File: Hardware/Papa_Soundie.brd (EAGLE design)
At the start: 38.1 x 63.5 mm, 79 parts, among them J1 Audio Jack, J2 MICRO-SD_CARD_SOCKET, U1 ATMEGA328P_TQFP, U2 VS1000D, U3 3.3V, U4 4MB Flash, Y1 12MHz, Y2 8MHz

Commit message: final layout
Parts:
- J6: device SparkFun-Connectors:1X07 -> SparkFun-Connectors:1X05
- J8: device SparkFun-Connectors:1X04 -> SparkFun-Connectors:1X02
- moved LOGO6 87.6 mm to (30.9, 42.6), turned to 0 degrees
- moved LOGO1 87.1 mm to (19.0, 31.2), turned to 0 degrees
- moved LOGO2 66.6 mm to (33.5, 4.06)
- moved J7 48.5 mm to (1.27, 44.5)
- moved J8 39.8 mm to (1.27, 57.1), turned to 270 degrees
- moved J5 38.7 mm to (36.8, 31.8), turned to 90 degrees
- moved J10 37.8 mm to (36.8, 26.7)
- moved J11 37.8 mm to (36.8, 21.6)
- moved J3 37.8 mm to (36.8, 16.5)
- moved C16 27.1 mm to (8.10, 61.6), turned to 0 degrees
- moved R16 26.2 mm to (30.8, 24.0), turned to 180 degrees
- moved R32 24.2 mm to (23.3, 42.1), turned to 90 degrees
- moved LOGO3 24.1 mm to (35.7, 12.2)
- moved Y1 23.4 mm to (31.9, 37.8), turned to 180 degrees
- moved S1 22.8 mm to (8.73, 43.0), turned to 0 degrees
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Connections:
- removed net A2: J8.3, U1.25
- removed net A3: J8.4, U1.26
- removed net D7: J6.7, U1.11
- removed net D8: J6.6, U1.12
- net USBN: now also J10.2; no longer J10.1
- net USBP: now also J10.1; no longer J10.2
- net VS_RX: now also J11.2; no longer J11.1
- net VS_TX: now also J11.1; no longer J11.2
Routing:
- net VCC: track 69.4 -> 173.9 mm, vias 4 -> 13
- net DVDD: track 43.1 -> 131.8 mm, vias 0 -> 6
- net SCL: track 66.5 -> 12.6 mm, vias 1 -> 0
- net SDA: track 60.1 -> 10.9 mm, vias 1 -> 0
- net RAW: track 27.2 -> 70.1 mm, vias 1 -> 2
- net L_AC: track 57.1 -> 17.2 mm, vias 1 -> 0
- net D7: track 36.5 -> 0.00 mm
- net LEFT: track 6.05 -> 41.1 mm
- net D8: track 33.9 -> 0.00 mm
- net RIGHT: track 5.89 -> 37.2 mm, vias 0 -> 2
- net N$31: track 25.9 -> 54.6 mm, vias 2 -> 4
- net USBN: track 0.87 -> 26.9 mm, vias 0 -> 2
- net A2: track 24.6 -> 0.00 mm
- net GBUF: track 27.8 -> 3.68 mm, vias 2 -> 0
- net A3: track 24.0 -> 0.00 mm
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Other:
- board text added: "3.3V"
- board text added: "LEFT_AC"
- board text added: "MISO D12"
- board text added: "MOSI D11"
- board text added: "RIGHT_AC"
- board text added: "RST"
- board text added: "RX"
- board text added: "SCK D13"
- board text added: "TX"
- board text added: "UN"
- board text added: "UP"
- board text added: "USBN"
- board text added: "USBP"
- board text added: "VS_RX"
- board text added: "VS_TX"
- board text removed: "3.3"
- board text removed: "3.6-5.5v"
- board text removed: "A2"
- board text removed: "A3"
- board text removed: "AUDIO PLAYER"
- board text removed: "D11"
- board text removed: "D12"
- board text removed: "D13"
- board text removed: "D7"
- board text removed: "D8"
- board text removed: "LIL' SOUNDIE"
- board text removed: "MISO"
- board text removed: "MOSI"
- board text removed: "RESET"
- board text removed: "SCK"
- board text removed: "VCC"
- board text removed: "~"

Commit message: added pull-up resistor on XCS line
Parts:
- added R25: 100k, SparkFun-Resistors:0603-RES
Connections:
- net DVDD: now also R25.2
- net XCS: now also R25.1
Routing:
- net DVDD: track 131.8 -> 134.2 mm
- net XCS: track 24.3 -> 23.5 mm
- net GND: vias 53 -> 54
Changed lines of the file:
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@@
 <element name="J5" library="SparkFun-Connectors" package="1X02" value="" x="36.83" y="31.75" rot="R90"/>
 <element name="J10" library="SparkFun-Connectors" package="1X02" value="" x="36.83" y="26.67" rot="R90"/>
+<element name="R25" library="SparkFun-Resistors" package="0603-RES" value="100k" x="23.33625" y="22.86">
+<attribute name="PROD_ID" value="RES-07828" x="23.33625" y="22.86" size="1.778" layer="27" display="off"/>
+</element>
 </elements>
 <signals>
@@
 <via x="20.47875" y="26.67" extent="1-16" drill="0.381"/>
 <via x="23.8125" y="25.24125" extent="1-16" drill="0.381"/>
-<via x="23.1775" y="22.38375" extent="1-16" drill="0.381"/>
+<via x="22.38375" y="21.11375" extent="1-16" drill="0.381"/>
 <via x="34.925" y="22.70125" extent="1-16" drill="0.381"/>
 <via x="32.22625" y="57.30875" extent="1-16" drill="0.381"/>
@@
 <via x="1.27" y="42.38625" extent="1-16" drill="0.381"/>
 <via x="0.79375" y="20.79625" extent="1-16" drill="0.381"/>
+<via x="19.05" y="20.32" extent="1-16" drill="0.381"/>
 </signal>
 <signal name="PWRBTN">
@@
 <wire x1="19.685" y1="16.8275" x2="20.0025" y2="17.145" width="0.2032" layer="1"/>
 <wire x1="20.0025" y1="17.145" x2="20.955" y2="17.145" width="0.2032" layer="1"/>
-<wire x1="20.955" y1="17.145" x2="25.55875" y2="21.74875" width="0.2032" layer="1"/>
+<wire x1="20.955" y1="17.145" x2="24.4475" y2="20.6375" width="0.2032" layer="1"/>
+<wire x1="24.4475" y1="20.6375" x2="25.55875" y2="21.74875" width="0.2032" layer="1"/>
 <wire x1="18.57375" y1="17.93875" x2="19.685" y2="16.8275" width="0.2032" layer="1"/>
 <wire x1="17.93875" y1="19.31125" x2="17.93875" y2="17.93875" width="0.2032" layer="1"/>
@@
 <wire x1="21.0775" y1="33.56375" x2="22.56" y2="33.56375" width="0.2032" layer="1"/>
 <wire x1="22.56" y1="33.56375" x2="22.77125" y2="33.775" width="0.2032" layer="1"/>
+<contactref element="R25" pad="2"/>
+<wire x1="24.18625" y1="22.86" x2="24.18625" y2="20.89875" width="0.2032" layer="1"/>
+<wire x1="24.18625" y1="20.89875" x2="24.4475" y2="20.6375" width="0.2032" layer="1"/>
 </signal>
 <signal name="N$2">
@@
 <wire x1="18.0775" y1="29.56375" x2="18.0775" y2="28.595" width="0.2032" layer="1"/>
 <wire x1="18.0775" y1="28.595" x2="18.57375" y2="28.09875" width="0.2032" layer="1"/>
-<via x="19.52625" y="23.495" extent="1-16" drill="0.381"/>
+<via x="19.3675" y="23.33625" extent="1-16" drill="0.381"/>
 <via x="10.16" y="22.38375" extent="1-16" drill="0.381"/>
 <wire x1="10.16" y1="22.38375" x2="10.16" y2="21.17" width="0.2032" layer="1"/>
@@
 <wire x1="10.16" y1="22.38375" x2="10.16" y2="27.305" width="0.2032" layer="16"/>
 <wire x1="10.16" y1="27.305" x2="10.4775" y2="27.6225" width="0.2032" layer="16"/>
-<wire x1="18.57375" y1="28.09875" x2="18.57375" y2="24.4475" width="0.2032" layer="1"/>
-<wire x1="18.57375" y1="24.4475" x2="19.52625" y2="23.495" width="0.2032" layer="1"/>
-<wire x1="18.0975" y1="24.92375" x2="19.52625" y2="23.495" width="0.2032" layer="16"/>
-<wire x1="18.0975" y1="24.92375" x2="18.0975" y2="27.14625" width="0.2032" layer="16"/>
+<wire x1="18.57375" y1="28.09875" x2="18.57375" y2="24.13" width="0.2032" layer="1"/>
+<wire x1="18.0975" y1="24.60625" x2="18.0975" y2="27.14625" width="0.2032" layer="16"/>
 <wire x1="18.0975" y1="27.14625" x2="17.62125" y2="27.6225" width="0.2032" layer="16"/>
 <wire x1="17.62125" y1="27.6225" x2="10.4775" y2="27.6225" width="0.2032" layer="16"/>
+<wire x1="18.57375" y1="24.13" x2="19.3675" y2="23.33625" width="0.2032" layer="1"/>
+<wire x1="18.0975" y1="24.60625" x2="19.3675" y2="23.33625" width="0.2032" layer="16"/>
 </signal>
 <signal name="IO_0">
@@
 <wire x1="18.5775" y1="29.56375" x2="18.5775" y2="28.73" width="0.2032" layer="1"/>
 <wire x1="18.5775" y1="28.73" x2="19.20875" y2="28.09875" width="0.2032" layer="1"/>
-<wire x1="19.20875" y1="28.09875" x2="19.20875" y2="24.92375" width="0.2032" layer="1"/>
-<via x="21.74875" y="23.01875" extent="1-16" drill="0.381"/>
+<via x="20.79625" y="24.4475" extent="1-16" drill="0.381"/>
 <via x="25.0825" y="30.12375" extent="1-16" drill="0.381"/>
 <wire x1="27.26725" y1="30.00375" x2="27.33075" y2="30.06725" width="0.2032" layer="1"/>
 <wire x1="23.8125" y1="30.00375" x2="21.9075" y2="28.09875" width="0.2032" layer="16"/>
-<wire x1="20.955" y1="23.8125" x2="21.74875" y2="23.01875" width="0.2032" layer="16"/>
-<wire x1="19.20875" y1="24.92375" x2="19.52625" y2="24.60625" width="0.2032" layer="1"/>
-<wire x1="19.52625" y1="24.60625" x2="20.16125" y2="24.60625" width="0.2032" layer="1"/>
-<wire x1="20.16125" y1="24.60625" x2="21.74875" y2="23.01875" width="0.2032" layer="1"/>
 <wire x1="21.9075" y1="28.09875" x2="19.52625" y2="28.09875" width="0.2032" layer="16"/>
 <wire x1="19.52625" y1="28.09875" x2="19.20875" y2="27.78125" width="0.2032" layer="16"/>
-<wire x1="19.20875" y1="27.78125" x2="19.20875" y2="25.55875" width="0.2032" layer="16"/>
-<wire x1="19.20875" y1="25.55875" x2="21.74875" y2="23.01875" width="0.2032" layer="16"/>
 <wire x1="23.8125" y1="30.00375" x2="24.9625" y2="30.00375" width="0.2032" layer="16"/>
 <wire x1="24.9625" y1="30.00375" x2="25.0825" y2="30.12375" width="0.2032" layer="16"/>
 <wire x1="27.26725" y1="30.00375" x2="25.2025" y2="30.00375" width="0.2032" layer="1"/>
 <wire x1="25.2025" y1="30.00375" x2="25.0825" y2="30.12375" width="0.2032" layer="1"/>
+<contactref element="R25" pad="1"/>
+<wire x1="21.2725" y1="22.86" x2="22.48625" y2="22.86" width="0.2032" layer="1"/>
+<wire x1="19.20875" y1="24.92375" x2="19.685" y2="24.4475" width="0.2032" layer="16"/>
+<wire x1="21.2725" y1="22.86" x2="20.955" y2="23.1775" width="0.2032" layer="1"/>
+<wire x1="20.955" y1="23.1775" x2="20.955" y2="24.28875" width="0.2032" layer="1"/>
+<wire x1="20.955" y1="24.28875" x2="20.79625" y2="24.4475" width="0.2032" layer="1"/>
+<wire x1="19.20875" y1="27.78125" x2="19.20875" y2="24.92375" width="0.2032" layer="16"/>
+<wire x1="19.685" y1="24.4475" x2="20.79625" y2="24.4475" width="0.2032" layer="16"/>
+<wire x1="19.20875" y1="28.09875" x2="19.20875" y2="24.92375" width="0.2032" layer="1"/>
+<wire x1="19.20875" y1="24.92375" x2="19.605625" y2="24.526875" width="0.2032" layer="1"/>
+<wire x1="19.605625" y1="24.526875" x2="20.716875" y2="24.526875" width="0.2032" layer="1"/>
+<wire x1="20.716875" y1="24.526875" x2="20.79625" y2="24.4475" width="0.2032" layer="1"/>
 </signal>
 <signal name="SCLK">

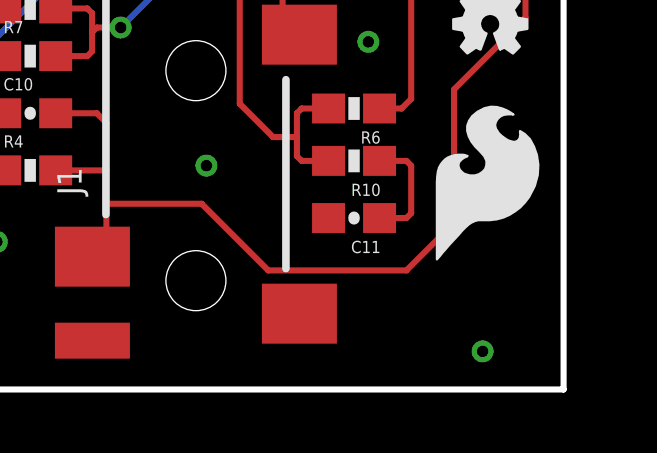
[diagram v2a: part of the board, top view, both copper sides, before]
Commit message: added measurement to third standoff
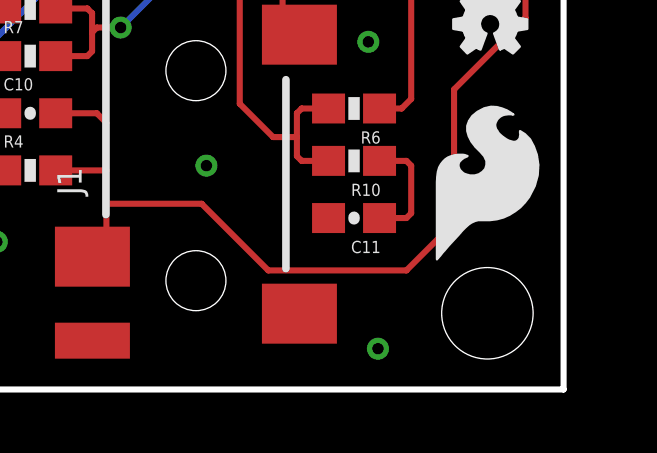
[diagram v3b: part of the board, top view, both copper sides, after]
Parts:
- added H3: STAND-OFFTIGHT, SparkFun-Electromechanical:STAND-OFF-TIGHT
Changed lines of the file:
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@@
 <setting verticaltext="up"/>
 </settings>
-<grid distance="0.00625" unitdist="inch" unit="inch" style="lines" multiple="1" display="yes" altdistance="0.01" altunitdist="mm" altunit="mm"/>
+<grid distance="0.05" unitdist="inch" unit="inch" style="lines" multiple="1" display="yes" altdistance="0.01" altunitdist="mm" altunit="mm"/>
 <layers>
 <layer number="1" name="Top" color="4" fill="1" visible="yes" active="yes"/>
@@
 <layer number="45" name="Holes" color="7" fill="1" visible="no" active="yes"/>
 <layer number="46" name="Milling" color="3" fill="1" visible="no" active="yes"/>
-<layer number="47" name="Measures" color="7" fill="1" visible="no" active="yes"/>
+<layer number="47" name="Measures" color="7" fill="1" visible="yes" active="yes"/>
 <layer number="48" name="Document" color="7" fill="1" visible="no" active="yes"/>
 <layer number="49" name="Reference" color="7" fill="1" visible="yes" active="yes"/>
@@
 <text x="28.32625" y="17.005" size="1.016" layer="22" font="vector" ratio="20" rot="MR180">RIGHT_AC</text>
 <wire x1="2.54" y1="58.26125" x2="2.69875" y2="58.26125" width="0.2032" layer="49"/>
+<dimension x1="35.56" y1="2.54" x2="38.1" y2="2.54" x3="36.83" y3="-3.81" textsize="1.778" layer="47" unit="inch"/>
 </plain>
 <attributes>
@@
 <attribute name="PROD_ID" value="RES-07828" x="23.33625" y="22.86" size="1.778" layer="27" display="off"/>
 </element>
+<element name="H3" library="SparkFun-Electromechanical" package="STAND-OFF-TIGHT" value="STAND-OFFTIGHT" x="35.56" y="2.54"/>
 </elements>
 <signals>
@@
 <via x="26.19375" y="7.46125" extent="1-16" drill="0.381"/>
 <via x="34.44875" y="15.875" extent="1-16" drill="0.381"/>
-<via x="35.40125" y="1.27" extent="1-16" drill="0.381"/>
+<via x="31.91125" y="1.36" extent="1-16" drill="0.381"/>
 <via x="14.605" y="46.6725" extent="1-16" drill="0.381"/>
 <via x="15.71625" y="49.05375" extent="1-16" drill="0.381"/>

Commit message: changes per QC Review
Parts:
- moved C4 17.3 mm to (16.3, 42.4), turned to 90 degrees
- moved C7 1.15 mm to (14.3, 42.4)
- moved R27 0.51 mm to (18.0, 42.2)
- moved C15 0.38 mm to (19.7, 42.2)
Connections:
- net AVDD: now also C4.1
- net VCC: no longer C4.1
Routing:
- net N$2: track 4.15 -> 0.00 mm
- net VCC: track 173.9 -> 171.9 mm
- net AVDD: track 13.6 -> 15.0 mm
- net N$7: track 3.39 -> 3.99 mm
- net GBUF: track 3.68 -> 4.19 mm
- net GND: vias 54 -> 55

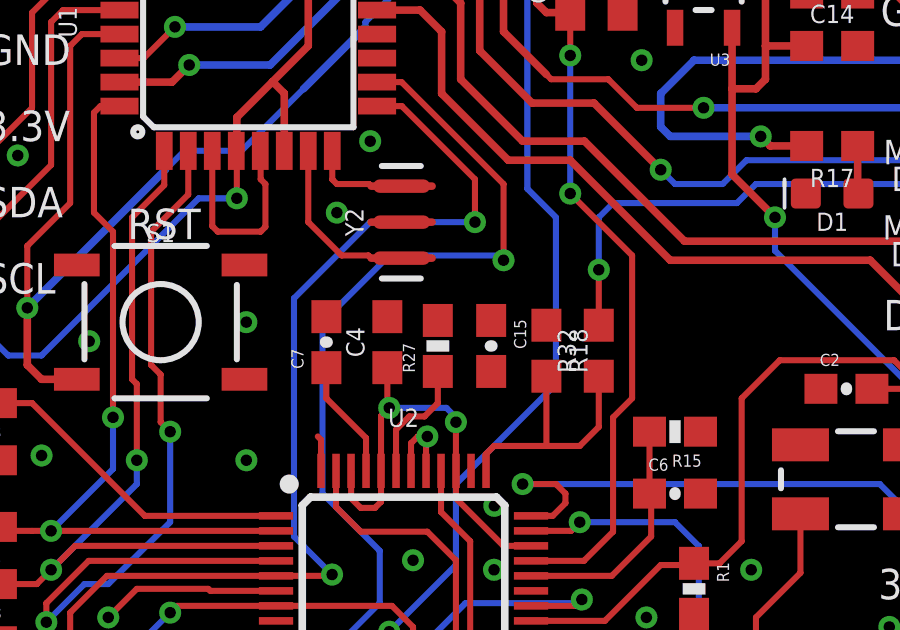
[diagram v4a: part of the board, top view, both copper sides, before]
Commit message: Fixing issues per QC review
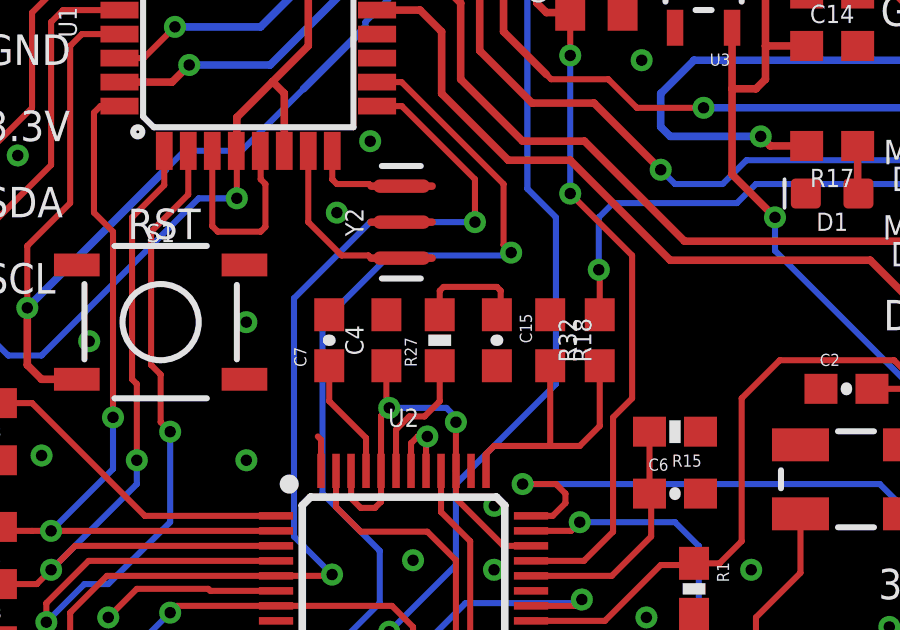
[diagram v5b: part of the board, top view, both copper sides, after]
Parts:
- moved R18 0.37 mm to (21.7, 42.4)
- moved R32 0.35 mm to (23.4, 42.4)
- moved C15 0.27 mm to (19.9, 42.4)
- moved R27 0.20 mm to (18.0, 42.4)
- moved C7 0.11 mm to (14.4, 42.4)
- moved C4 0.07 mm to (16.3, 42.4)
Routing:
- net N$2: track 0.00 -> 3.79 mm
- net PWRBTN: track 8.71 -> 9.42 mm

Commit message: Updated design for rev 2
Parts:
- removed C27: 1.0uF, SparkFun-Capacitors:0603
- removed R32: 39k, SparkFun-Resistors:0603
- added D2, D3: RED, SparkFun-LED:LED-0603
- added J12: (no value), SparkFun-Connectors:1X01
- added R26: 2.0k, SparkFun-Resistors:0603
- R18: value 68.1k -> 2.0k
- moved R18 18.2 mm to (8.64, 29.7), turned to 0 degrees
- moved FD3 5.97 mm to (5.71, 61.8)
- moved FD1 1.41 mm to (5.71, 61.8)
- moved R11 0.90 mm to (2.41, 25.8)
- moved R12 0.90 mm to (2.41, 35.3)
- moved R22 0.90 mm to (2.41, 23.9)
- moved R29 0.90 mm to (2.41, 31.5)
- moved R30 0.90 mm to (2.41, 29.6)
- moved R31 0.90 mm to (2.41, 27.7)
- moved C13 0.90 mm to (2.41, 39.4)
- moved R23 0.90 mm to (2.41, 37.5)
- moved R28 0.90 mm to (2.41, 33.4)
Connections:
- removed net N$60: C27.2, R32.2
- new net N$34: D2.C, R18.2
- new net N$35: D2.A, U2.10
- new net N$36: D3.C, R26.2
- new net RST: C8.2, J12.1, R9.1, S1.3, U1.29
- net GND: now also C3.2, J2.CD2, R26.1
- net N$31: now also D3.A, U1.25; no longer C8.2, R9.1, S1.3, U1.29
- net PWRBTN: now also U1.11; no longer R18.2, R32.1
- net RAW: no longer C27.1
- net SD3V3: no longer C3.2
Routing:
- net RST: track 0.00 -> 58.2 mm, vias 0 -> 4
- net N$31: track 54.6 -> 6.72 mm, vias 4 -> 0
- net N$60: track 23.7 -> 0.00 mm, vias 2 -> 0
- net PWRBTN: track 9.42 -> 18.8 mm, vias 0 -> 2
- net N$35: track 0.00 -> 3.28 mm
- net RAW: track 70.1 -> 67.7 mm
- net N$34: track 0.00 -> 2.23 mm
- net GND: track 26.2 -> 28.0 mm, vias 55 -> 56
- net IO_4: track 42.0 -> 43.5 mm
- net N$36: track 0.00 -> 1.45 mm
- net A0: track 10.7 -> 11.7 mm, vias 0 -> 1
- net SD3V3: track 38.9 -> 37.8 mm
- net IO_3: track 36.4 -> 37.4 mm
- net IO_6: track 12.2 -> 12.8 mm
- net IO_7: track 12.8 -> 13.4 mm
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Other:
- board text added: "RDY"
- board text added: "VLSI RDY"
- board text added: "v03"
- board text removed: "v02"

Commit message: Updated Version No., removed ground connection from SD Card, v03
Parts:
- moved LOGO3 35.9 mm to (8.60, 35.8)
- moved LOGO2 32.3 mm to (7.24, 22.9)
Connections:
- net GND: no longer J2.CD2

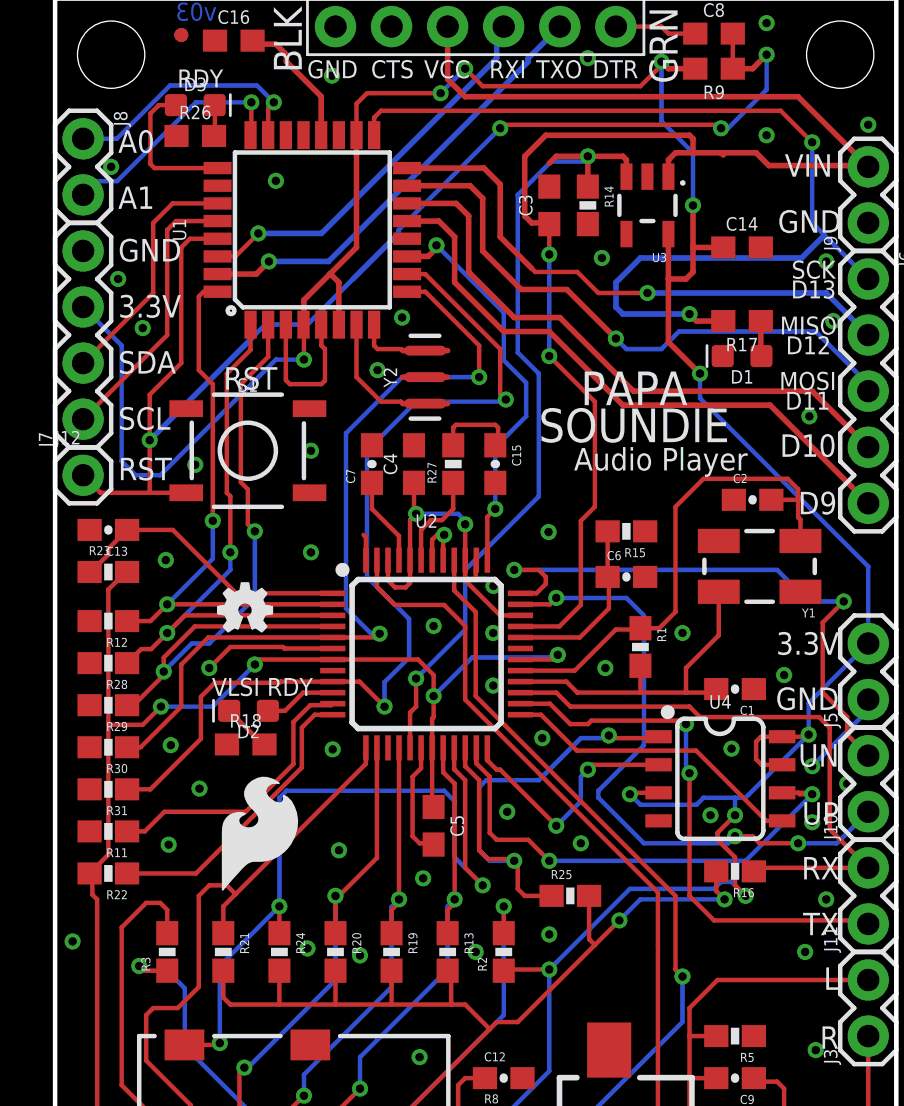
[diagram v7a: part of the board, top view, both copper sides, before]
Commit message: fixing enable line, SD3V3
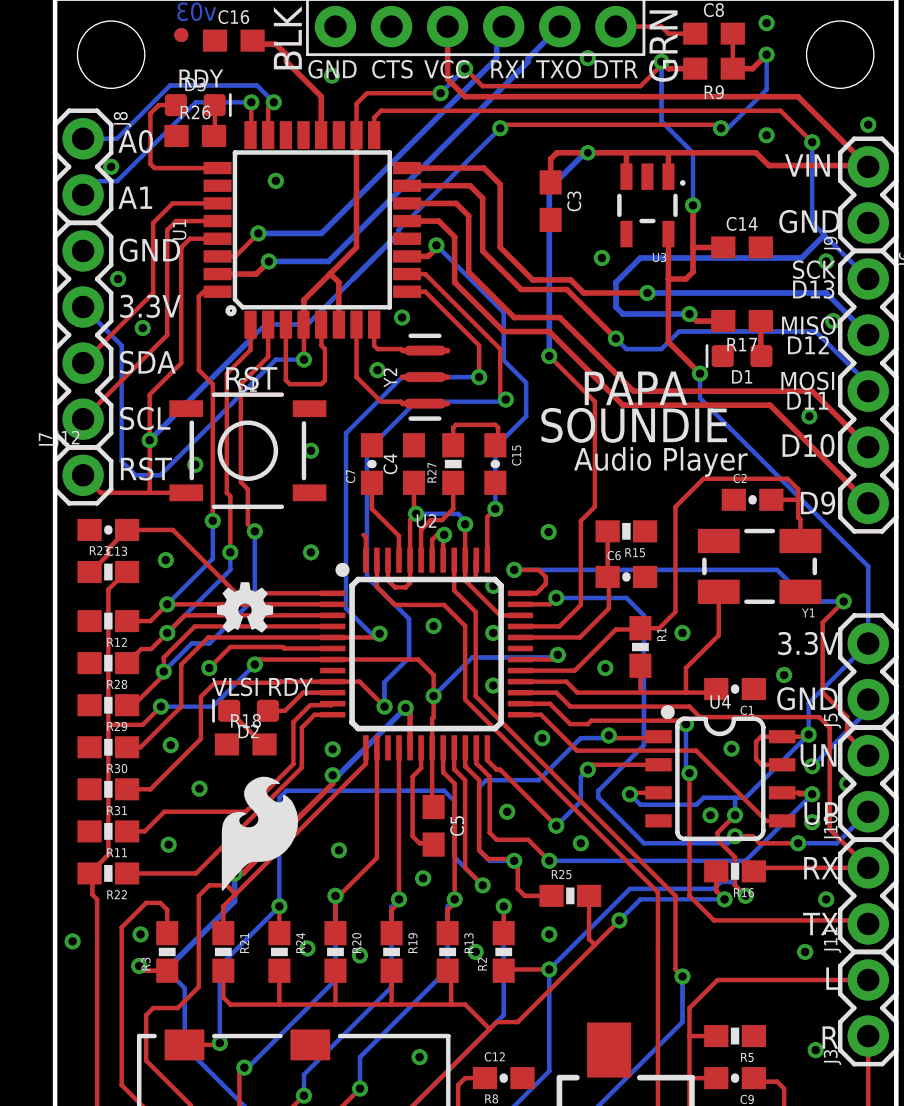
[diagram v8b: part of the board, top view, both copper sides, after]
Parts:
- removed R14: 100k, SparkFun-Resistors:0603-RES
- moved C3 0.20 mm to (22.4, 54.3), turned to 270 degrees
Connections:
- removed net SD3V3: R14.1, U2.17, U3.3
- net GND: no longer R14.2
- net RAW: now also U3.3
- net VCC: now also U2.17
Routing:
- net SD3V3: track 37.8 -> 0.00 mm, vias 2 -> 0
- net VCC: track 171.9 -> 190.6 mm, vias 13 -> 16
- net RAW: track 67.7 -> 66.5 mm
- net GND: vias 56 -> 57
